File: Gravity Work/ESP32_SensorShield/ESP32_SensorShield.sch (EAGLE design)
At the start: 45 parts, among them IC1 BMP388, J7 2X6 FEMALE, U1 FGPMMOPA6H, U2 MB85RC256VPF-G-JNERE2, U3 SPX3819-3.3, U4 SN65HVD230D, Y1 32.768kHz

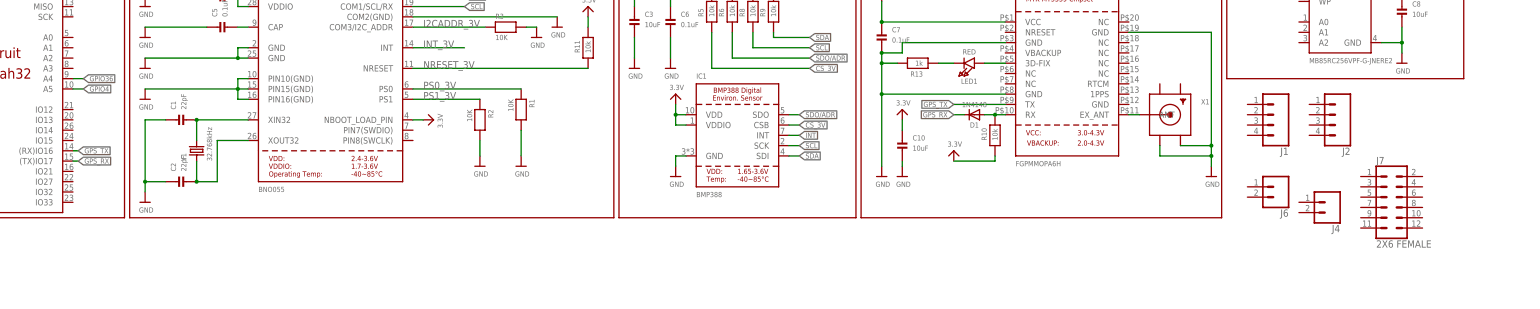
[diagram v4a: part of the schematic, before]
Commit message: Moved Holes/LED around, modfied SPI Pins,began routing.
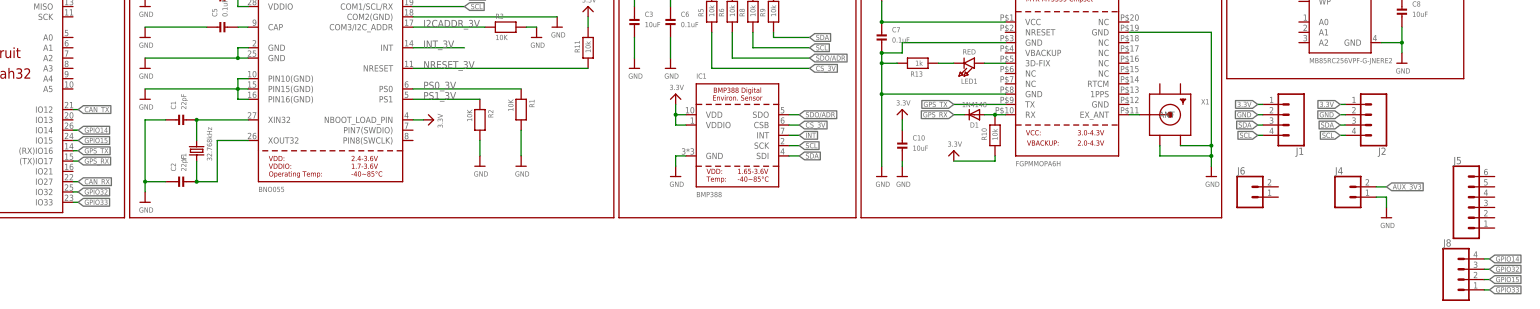
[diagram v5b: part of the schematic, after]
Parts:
- removed J7: 2X6 FEMALE, SparkFun-Connectors:CONN_06X2PTH_FEMALE
- added J5: (no value), SparkFun-Connectors:CONN_06SILK_FEMALE_PTH
- added J8: (no value), SparkFun-Connectors:CONN_04
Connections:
- removed net GPIO36: U$1.A4
- removed net GPIO4: U$1.A5
- new net GPIO14: J8.4, U$1.IO14
- new net GPIO15: J8.2, U$1.IO15
- new net GPIO32: J8.3, U$1.IO32
- new net GPIO33: J8.1, U$1.IO33
- net 3.3V: now also J1.1, J2.1
- net AUX_3V3: now also J4.2
- net CAN_RX: now also U$1.IO27
- net CAN_TX: now also U$1.IO12
- net GND: now also J1.2, J2.2, J4.1
- net SCL: now also J1.4, J2.4
- net SDA: now also J1.3, J2.3
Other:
- moved on the sheet: J1, J2, J4, J6

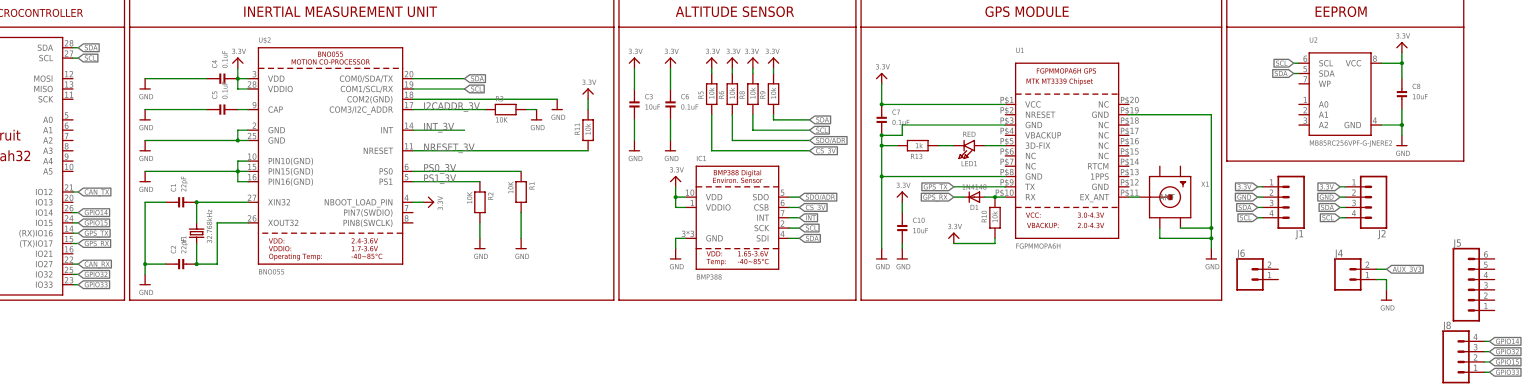
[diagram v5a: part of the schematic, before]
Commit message: Completed a large portion of routing
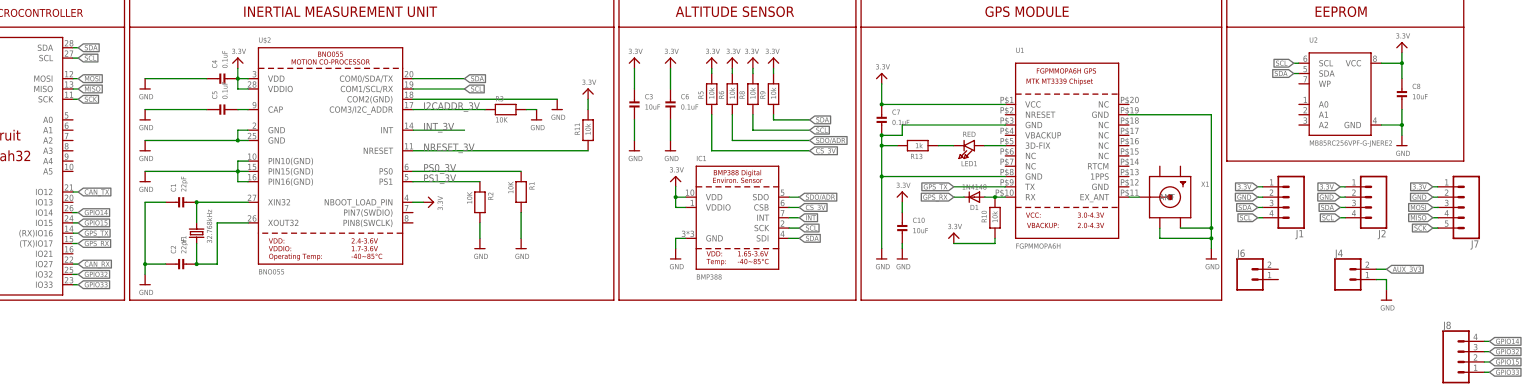
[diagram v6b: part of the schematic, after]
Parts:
- removed J5: (no value), SparkFun-Connectors:CONN_06SILK_FEMALE_PTH
- added J7: (no value), SparkFun-Connectors:CONN_05
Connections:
- new net MISO: J7.4, U$1.MISO
- new net MOSI: J7.3, U$1.MOSI
- new net SCK: J7.5, U$1.SCK
- net 3.3V: now also J7.1
- net GND: now also J7.2
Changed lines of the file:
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@@
 <part name="J4" library="SparkFun-Connectors" library_urn="urn:adsk.eagle:library:513" deviceset="CONN_02" device="" package3d_urn="urn:adsk.eagle:package:38039/1"/>
 <part name="U$36" library="Particle" deviceset="RGB-LED-CLMVB-FKA" device="RGB"/>
-<part name="J5" library="SparkFun-Connectors" library_urn="urn:adsk.eagle:library:513" deviceset="CONN_06" device="SILK_FEMALE_PTH" package3d_urn="urn:adsk.eagle:package:38009/1"/>
 <part name="J8" library="SparkFun-Connectors" library_urn="urn:adsk.eagle:library:513" deviceset="CONN_04" device="" package3d_urn="urn:adsk.eagle:package:38085/1"/>
 <part name="U$37" library="microbuilder" deviceset="GND" device=""/>
+<part name="J7" library="SparkFun-Connectors" library_urn="urn:adsk.eagle:library:513" deviceset="CONN_05" device="" package3d_urn="urn:adsk.eagle:package:38104/1"/>
 </parts>
 <sheets>
@@
 <instance part="J4" gate="G$1" x="354.33" y="5.08"/>
 <instance part="U$36" gate="G$1" x="157.48" y="105.41"/>
-<instance part="J5" gate="G$1" x="386.08" y="2.54"/>
 <instance part="J8" gate="G$1" x="383.54" y="-15.24"/>
 <instance part="U$37" gate="G$1" x="364.49" y="0"/>
+<instance part="J7" gate="G$1" x="384.81" y="22.86" rot="R180"/>
 </instances>
 <busses>
@@
 <wire x1="364.49" y1="5.08" x2="364.49" y2="2.54" width="0.1524" layer="91"/>
 </segment>
+<segment>
+<pinref part="J7" gate="G$1" pin="2"/>
+<wire x1="377.19" y1="25.4" x2="375.92" y2="25.4" width="0.1524" layer="91"/>
+<label x="375.92" y="25.4" size="1.27" layer="95" rot="R180" xref="yes"/>
+</segment>
 </net>
 <net name="3.3V" class="0">
@@
 <wire x1="354.33" y1="27.94" x2="353.06" y2="27.94" width="0.1524" layer="91"/>
 <label x="353.06" y="27.94" size="1.27" layer="95" rot="R180" xref="yes"/>
+</segment>
+<segment>
+<pinref part="J7" gate="G$1" pin="1"/>
+<wire x1="377.19" y1="27.94" x2="375.92" y2="27.94" width="0.1524" layer="91"/>
+<label x="375.92" y="27.94" size="1.27" layer="95" rot="R180" xref="yes"/>
 </segment>
 </net>
@@
 </segment>
 </net>
+<net name="MISO" class="0">
+<segment>
+<pinref part="U$1" gate="G$1" pin="MISO"/>
+<wire x1="40.64" y1="52.07" x2="41.91" y2="52.07" width="0.1524" layer="91"/>
+<label x="41.91" y="52.07" size="1.27" layer="95" xref="yes"/>
+</segment>
+<segment>
+<pinref part="J7" gate="G$1" pin="4"/>
+<wire x1="377.19" y1="20.32" x2="375.92" y2="20.32" width="0.1524" layer="91"/>
+<label x="375.92" y="20.32" size="1.27" layer="95" rot="R180" xref="yes"/>
+</segment>
+</net>
+<net name="MOSI" class="0">
+<segment>
+<pinref part="U$1" gate="G$1" pin="MOSI"/>
+<wire x1="40.64" y1="54.61" x2="41.91" y2="54.61" width="0.1524" layer="91"/>
+<label x="41.91" y="54.61" size="1.27" layer="95" xref="yes"/>
+</segment>
+<segment>
+<pinref part="J7" gate="G$1" pin="3"/>
+<wire x1="377.19" y1="22.86" x2="375.92" y2="22.86" width="0.1524" layer="91"/>
+<label x="375.92" y="22.86" size="1.27" layer="95" rot="R180" xref="yes"/>
+</segment>
+</net>
+<net name="SCK" class="0">
+<segment>
+<pinref part="J7" gate="G$1" pin="5"/>
+<wire x1="377.19" y1="17.78" x2="375.92" y2="17.78" width="0.1524" layer="91"/>
+<label x="375.92" y="17.78" size="1.27" layer="95" rot="R180" xref="yes"/>
+</segment>
+<segment>
+<pinref part="U$1" gate="G$1" pin="SCK"/>
+<wire x1="40.64" y1="49.53" x2="41.91" y2="49.53" width="0.1524" layer="91"/>
+<label x="41.91" y="49.53" size="1.27" layer="95" xref="yes"/>
+</segment>
+</net>

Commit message: Completed Routing and Fixed DRC Errors. Need to Perfrom Final Check w/ Butch and Selfcheck.
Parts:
- removed J1, J2, J8: (no value), SparkFun-Connectors:CONN_04
- removed J4, J6: (no value), SparkFun-Connectors:CONN_02
- removed J7: (no value), SparkFun-Connectors:CONN_05
- added AUX_3V3, CAN: (no value), SparkFun-Connectors:CONN_02
- added CS, I2C1, I2C2: (no value), SparkFun-Connectors:CONN_04
- added R12, R14, R15: 1k, microbuilder:RESISTOR0603
- added SPI: (no value), SparkFun-Connectors:CONN_05
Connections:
- new net LED_B: R12.1, U$1.A5
- new net LED_G: R14.1, U$1.A4
- new net LED_R: R15.1, U$1.A3
- new net N$12: R12.2, U$36.2
- new net N$13: R14.2, U$36.3
- new net N$14: R15.2, U$36.4
- net 3.3V: now also I2C1.1, I2C2.1, SPI.1, U$36.1; no longer J1.1, J2.1, J7.1
- net AUX_3V3: now also AUX_3V3.2; no longer J4.2
- net CANH: now also CAN.2
- net CANL: now also CAN.1
- net GND: now also AUX_3V3.1, I2C1.2, I2C2.2, SPI.2; no longer J1.2, J2.2, J4.1, J7.2
- net GPIO14: now also CS.4; no longer J8.4
- net GPIO15: now also CS.2; no longer J8.2
- net GPIO32: now also CS.3; no longer J8.3
- net GPIO33: now also CS.1; no longer J8.1
- net MISO: now also SPI.4; no longer J7.4
- net MOSI: now also SPI.3; no longer J7.3
- net SCK: now also SPI.5; no longer J7.5
- net SCL: now also I2C1.4, I2C2.4; no longer J1.4, J2.4
- net SDA: now also I2C1.3, I2C2.3; no longer J1.3, J2.3
- net VUSB: now also U$1.5V_VUSB
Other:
- note added: "BREAKOUT HEADERS"
- note added: "STATUS LED"
- moved on the sheet: C8, U$36, U2

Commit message: Added CAN Resistor, GPS GND Line Connected, Fixed Decoup Cap Value for AUX 3V3, Fixed Switch to not extend board size
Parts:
- added R16: 120, microbuilder:RESISTOR0603
- C12: value 0.1uF -> 1uF
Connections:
- net CANH: now also R16.1
- net CANL: now also R16.2
- net GND: now also U1.GND@3, X1.GND1, X1.GND2
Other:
- moved on the sheet: C13, R7, U4
